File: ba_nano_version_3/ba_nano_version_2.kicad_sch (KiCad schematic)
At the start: 84 parts, among them J1 GPIO_0, J2 GPIO_1, Q1 2N3904, Q2 2N3904, SW1 , SW10 , SW11 , SW12 , SW13 , SW14 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

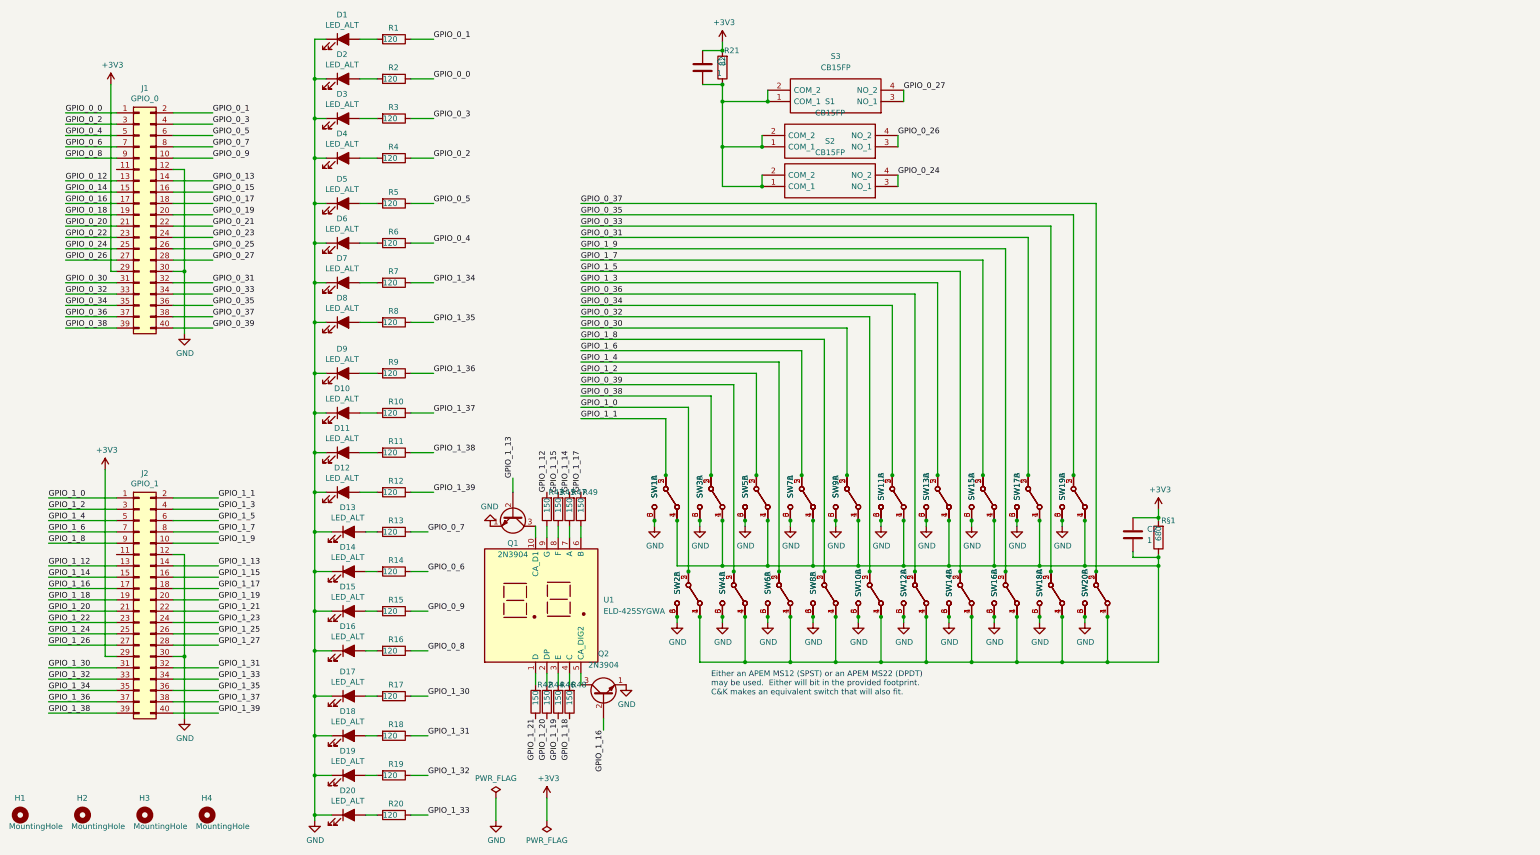
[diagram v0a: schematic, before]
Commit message: Made changes to KiCad schematic and CAD drawing. Changed SSDs and buttons
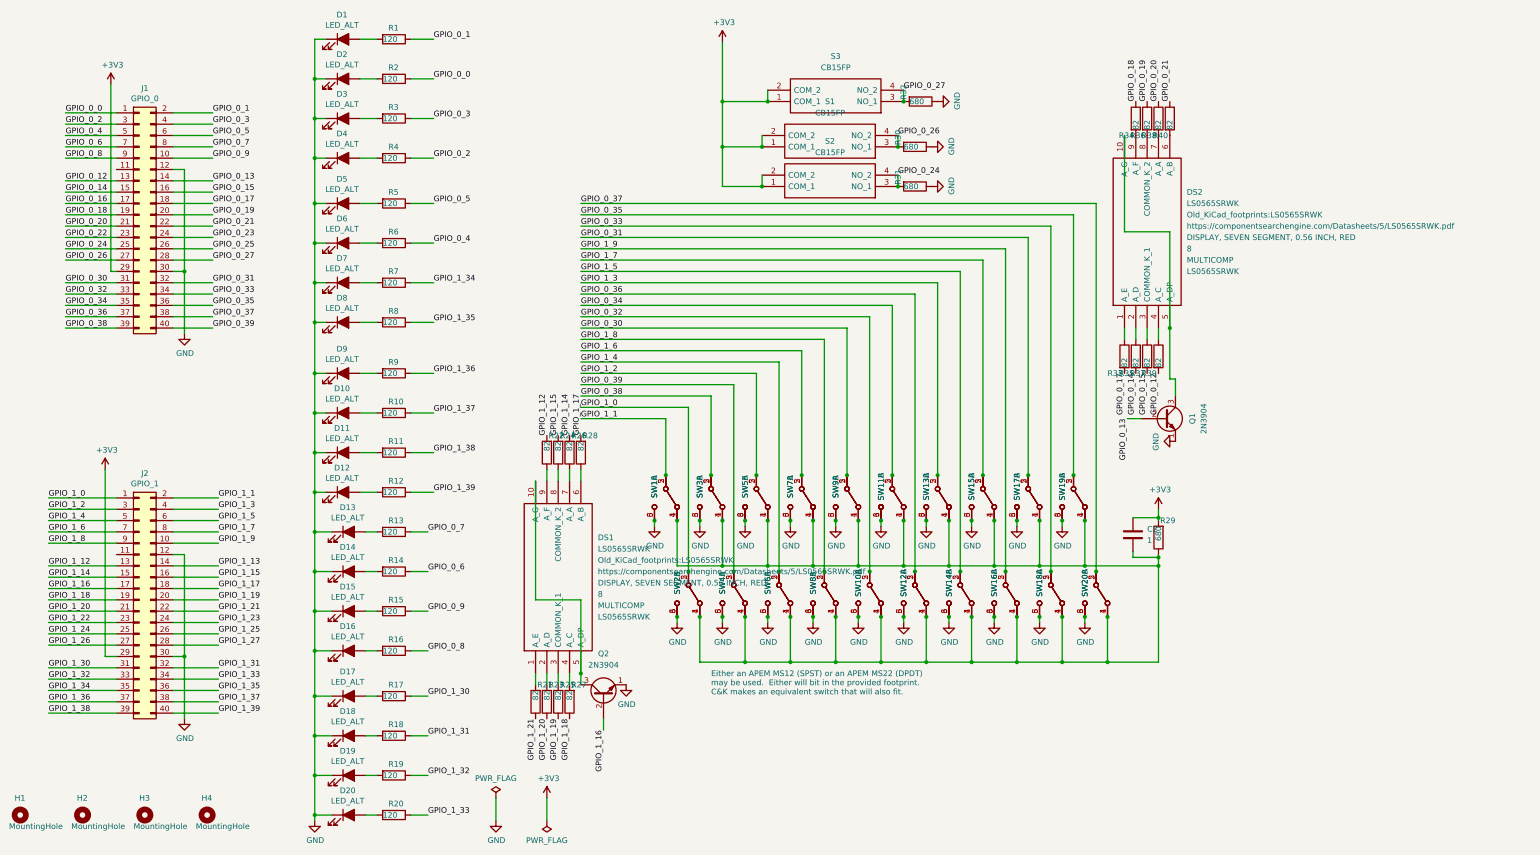
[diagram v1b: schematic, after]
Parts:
- removed C1: 1, Capacitor_SMD:C_2220_5650Metric, symbol Device:C
- removed R42, R43, R44, R45, R46, R47, R48, R49: 150, Resistor_SMD:R_0805_2012Metric_Pad1.20x1.40mm_HandSolder, symbol Device:R
- removed U1: ELD-425SYGWA, Old_KiCad_footprints:ELD-425SYGWA, symbol Extra_Parts:ELD-425SYGWA
- added DS1, DS2: LS0565SRWK, Old_KiCad_footprints:LS0565SRWK, symbol LS0565SRWK:LS0565SRWK
- added R22, R23, R24, R25, R26, R27, R28, R33, R34, R35, R36, R37, R38, R39, R40: 82, Resistor_SMD:R_1206_3216Metric, symbol Device:R
- added R30, R31, R32: 680, Resistor_SMD:R_1206_3216Metric, symbol Device:R
- R21: footprint Resistor_SMD:R_1210_3225Metric_Pad1.30x2.65mm_HandSolder -> Resistor_SMD:R_1206_3216Metric
- renumbered R§1 to R29
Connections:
- net +3V3: now also S1.1 (COM_1), S1.2 (COM_2), S2.1 (COM_1), S2.2 (COM_2), S3.1 (COM_1), S3.2 (COM_2); no longer R21.2
- net GND: now also R30.1, R31.1, R32.1
- net GPIO_0_12: now also R39.2
- net GPIO_0_13: now also Q1.2 (B)
- net GPIO_0_14: now also R35.2
- net GPIO_0_15: now also R37.2
- net GPIO_0_17: now also R33.2
- net GPIO_0_18: now also R34.1
- net GPIO_0_19: now also R36.1
- net GPIO_0_20: now also R38.1
- net GPIO_0_21: now also R40.1
- net GPIO_0_24: now also R31.2
- net GPIO_0_26: now also R30.2
- net GPIO_0_27: now also R32.2
- net GPIO_1_12: now also R22.2
- net GPIO_1_13: no longer Q1.2 (B)
- net GPIO_1_14: now also R26.2
- net GPIO_1_15: now also R24.2
- net GPIO_1_17: now also R28.2
- net GPIO_1_18: now also R27.1
- net GPIO_1_19: now also R25.1
- net GPIO_1_20: now also R23.1
- net GPIO_1_21: now also R21.1
- net at Q2.3 (C): now also DS1.10 (A_G), DS1.5 (A_DP)
- net at Q1.3 (C): now also DS2.10 (A_G), DS2.5 (A_DP)
- new net: DS1.8 (COMMON_K_2), R24.1
- new net: DS1.3 (COMMON_K_1), R25.2
- new net: DS1.6 (A_B), R28.1
- new net: DS1.4 (A_C), R27.2
- new net: DS2.1 (A_E), R33.1
- new net: DS2.4 (A_C), R39.1
- new net: DS1.1 (A_E), R21.2
- new net: DS1.2 (A_D), R23.2
- new net: DS1.7 (A_A), R26.1
- new net: DS1.9 (A_F), R22.1
- new net: DS2.3 (COMMON_K_1), R37.1
- new net: DS2.7 (A_A), R38.2
- new net: DS2.2 (A_D), R35.1
- new net: DS2.9 (A_F), R34.2
- new net: DS2.8 (COMMON_K_2), R36.2
- new net: DS2.6 (A_B), R40.2
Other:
- moved on the sheet: Q1

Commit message: Completed the adding of buttons and two independetely controlled SSDs
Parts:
- added R41: 680, Resistor_SMD:R_1206_3216Metric, symbol Device:R
- added S4: CB15FP, CB15FP:CB15FP, symbol CB15FP:CB15FP
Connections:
- net +3V3: now also S4.1 (COM_1), S4.2 (COM_2)
- net GND: now also R41.1
- net GPIO_0_12: now also R37.2; no longer R39.2
- net GPIO_0_13: now also R39.2; no longer Q1.2 (B)
- net GPIO_0_14: now also R33.2; no longer R35.2
- net GPIO_0_15: now also R35.2; no longer R37.2
- net GPIO_0_16: now also R30.2, S1.3 (NO_1), S1.4 (NO_2)
- net GPIO_0_17: now also R32.2, S3.3 (NO_1), S3.4 (NO_2); no longer R33.2
- net GPIO_0_18: no longer R34.1
- net GPIO_0_19: no longer R36.1
- net GPIO_0_20: no longer R38.1
- net GPIO_0_21: no longer R40.1
- net GPIO_0_22: now also R41.2, S4.3 (NO_1), S4.4 (NO_2)
- net GPIO_0_23: now also R31.2, S2.3 (NO_1), S2.4 (NO_2)
- net GPIO_0_24: now also R34.1; no longer R31.2, S2.3 (NO_1), S2.4 (NO_2)
- net GPIO_0_25: now also R36.1
- net GPIO_0_26: now also R38.1; no longer R30.2, S1.3 (NO_1), S1.4 (NO_2)
- net GPIO_0_27: now also R40.1; no longer R32.2, S3.3 (NO_1), S3.4 (NO_2)
- net GPIO_1_12: now also R24.2; no longer R22.2
- net GPIO_1_13: now also R22.2
- net GPIO_1_14: now also R28.2; no longer R26.2
- net GPIO_1_15: now also R26.2; no longer R24.2
- net GPIO_1_16: now also Q1.2 (B); no longer Q2.2 (B)
- net GPIO_1_17: now also Q2.2 (B); no longer R28.2
- net GPIO_1_18: no longer R27.1
- net GPIO_1_19: no longer R25.1
- net GPIO_1_20: no longer R23.1
- net GPIO_1_21: no longer R21.1
- net GPIO_1_24: now also R27.1
- net GPIO_1_25: now also R25.1
- net GPIO_1_26: now also R23.1
- net GPIO_1_27: now also R21.1
